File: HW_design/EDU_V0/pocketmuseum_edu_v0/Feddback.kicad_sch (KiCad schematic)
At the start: 18 parts

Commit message: Updated Readme
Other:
- company: (none) -> Bucharest Applied STEAM Museum
- title: (none) -> POCKETMUSEUM EDU V0
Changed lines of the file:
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@@
 	(generator_version "8.0")
 	(paper "A4")
+	(title_block
+		(title "POCKETMUSEUM EDU V0")
+		(date "2025-08-01")
+		(company "Bucharest Applied STEAM Museum")
+	)
 	(junction
 		(at 104.14 151.13)

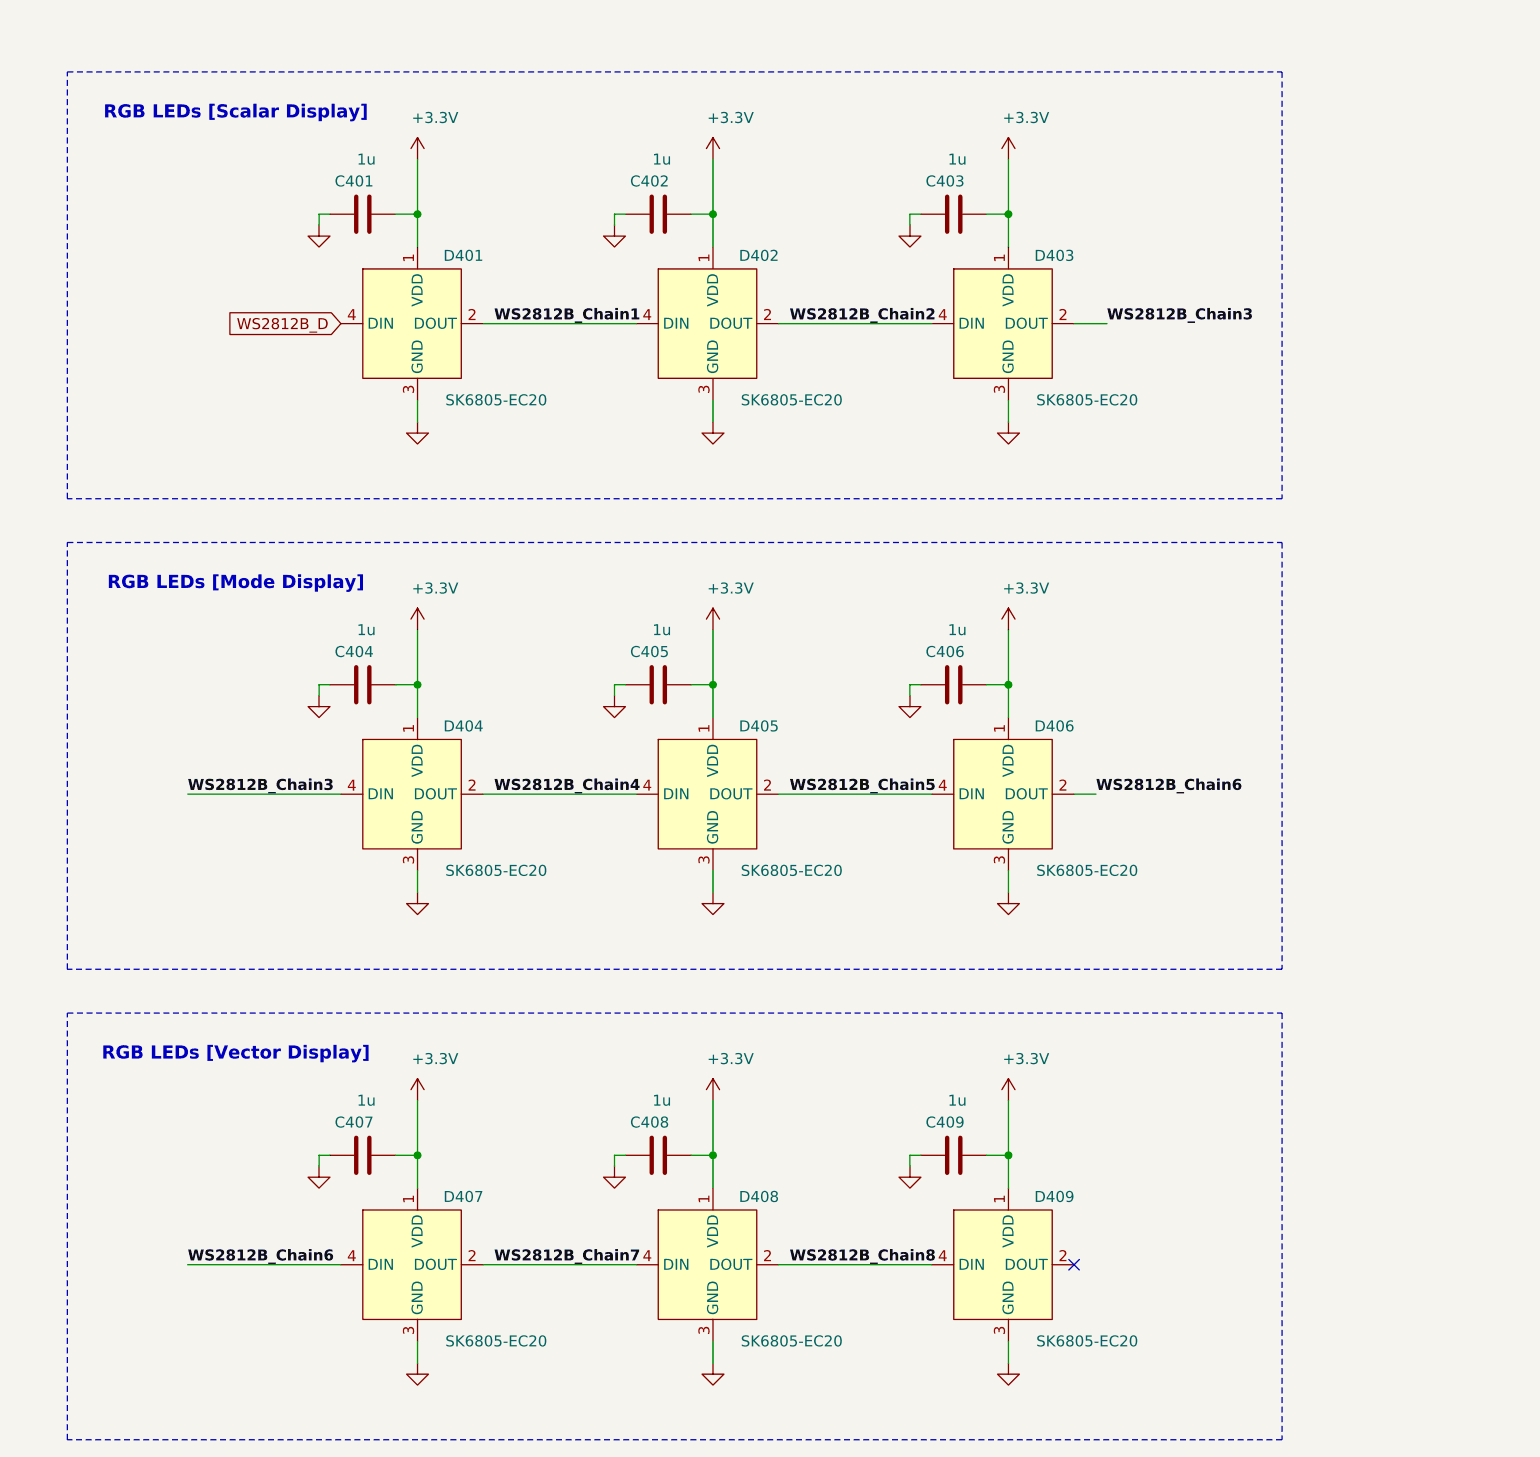
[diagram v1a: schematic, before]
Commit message: Added Mic & Light Sensor to EDU_V0
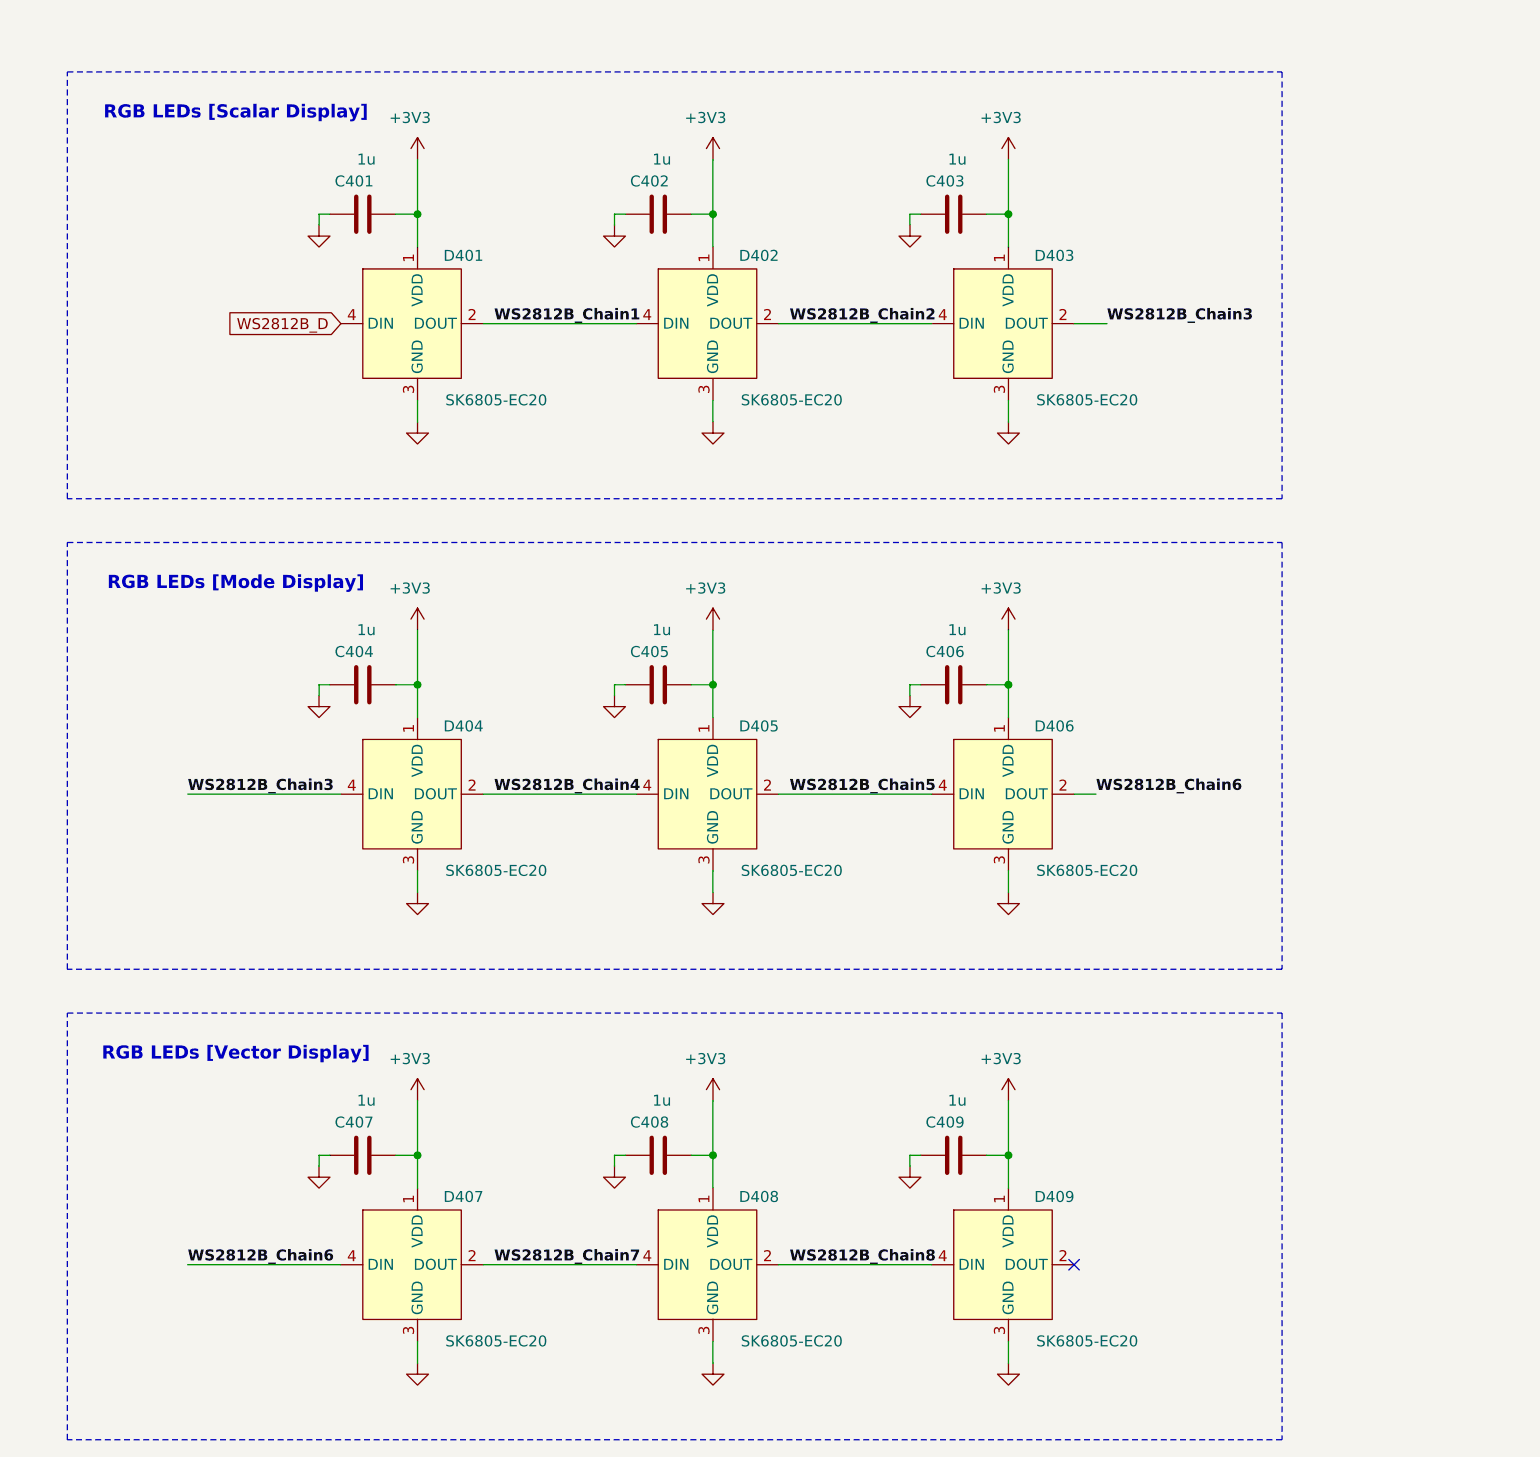
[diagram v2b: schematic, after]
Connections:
- net +3.3V renamed +3V3

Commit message: Diagram review complete
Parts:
- renumbered C404 to C401, C405 to C402, C401 to C403, C402 to C404, C403 to C405, D404 to D401, D405 to D402, D401 to D403, D402 to D404, D403 to D405
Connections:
- net WS2812B_Chain1: now also D401.2 (DOUT), D402.4 (DIN); no longer D403.2 (DOUT), D404.4 (DIN)
- net WS2812B_Chain2: now also D402.2 (DOUT), D403.4 (DIN); no longer D404.2 (DOUT), D405.4 (DIN)
- net WS2812B_Chain3: now also D403.2 (DOUT), D404.4 (DIN); no longer D401.4 (DIN), D405.2 (DOUT)
- net WS2812B_Chain4: now also D404.2 (DOUT), D405.4 (DIN); no longer D401.2 (DOUT), D402.4 (DIN)
- net WS2812B_Chain5: now also D405.2 (DOUT); no longer D402.2 (DOUT)
- net WS2812B_D: now also D401.4 (DIN); no longer D403.4 (DIN)
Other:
- note added: "RGB LEDs [Direction Display]"
- note added: "RGB LEDs [Magnitude Display]"
- note added: "RGB LEDs [Status Display]"
- note removed: "RGB LEDs [Mode Display]"
- note removed: "RGB LEDs [Scalar Display]"
- note removed: "RGB LEDs [Vector Display]"
- moved on the sheet: C401, C402, C403, C404, C405, C407, C408, C409, D401, D402, D403, D404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
